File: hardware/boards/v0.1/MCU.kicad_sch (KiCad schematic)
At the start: 38 parts, among them SW24 NRST, SW25 BOOT0, U1 BMDU, U18 STM32H743ZIT6, Y1 ECS-.327-12.5-1210-TR, Y4 8Q-25.000MEEV-T

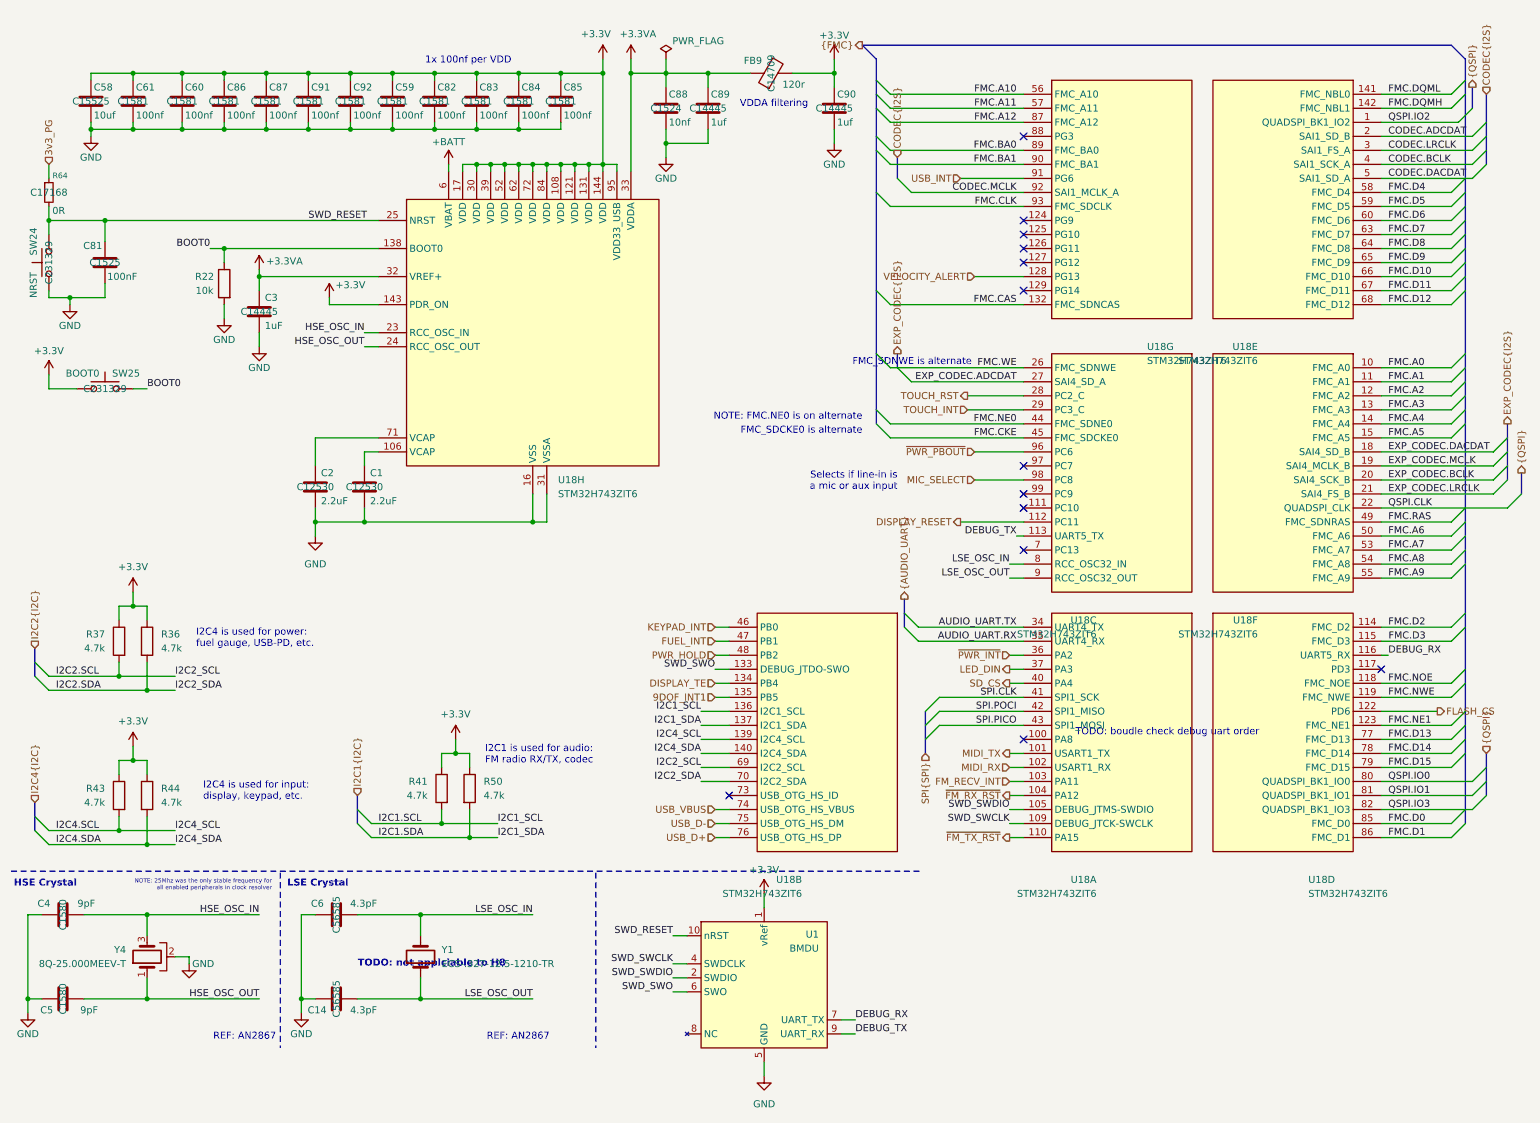
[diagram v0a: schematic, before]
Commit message: feat: update various components to 0402
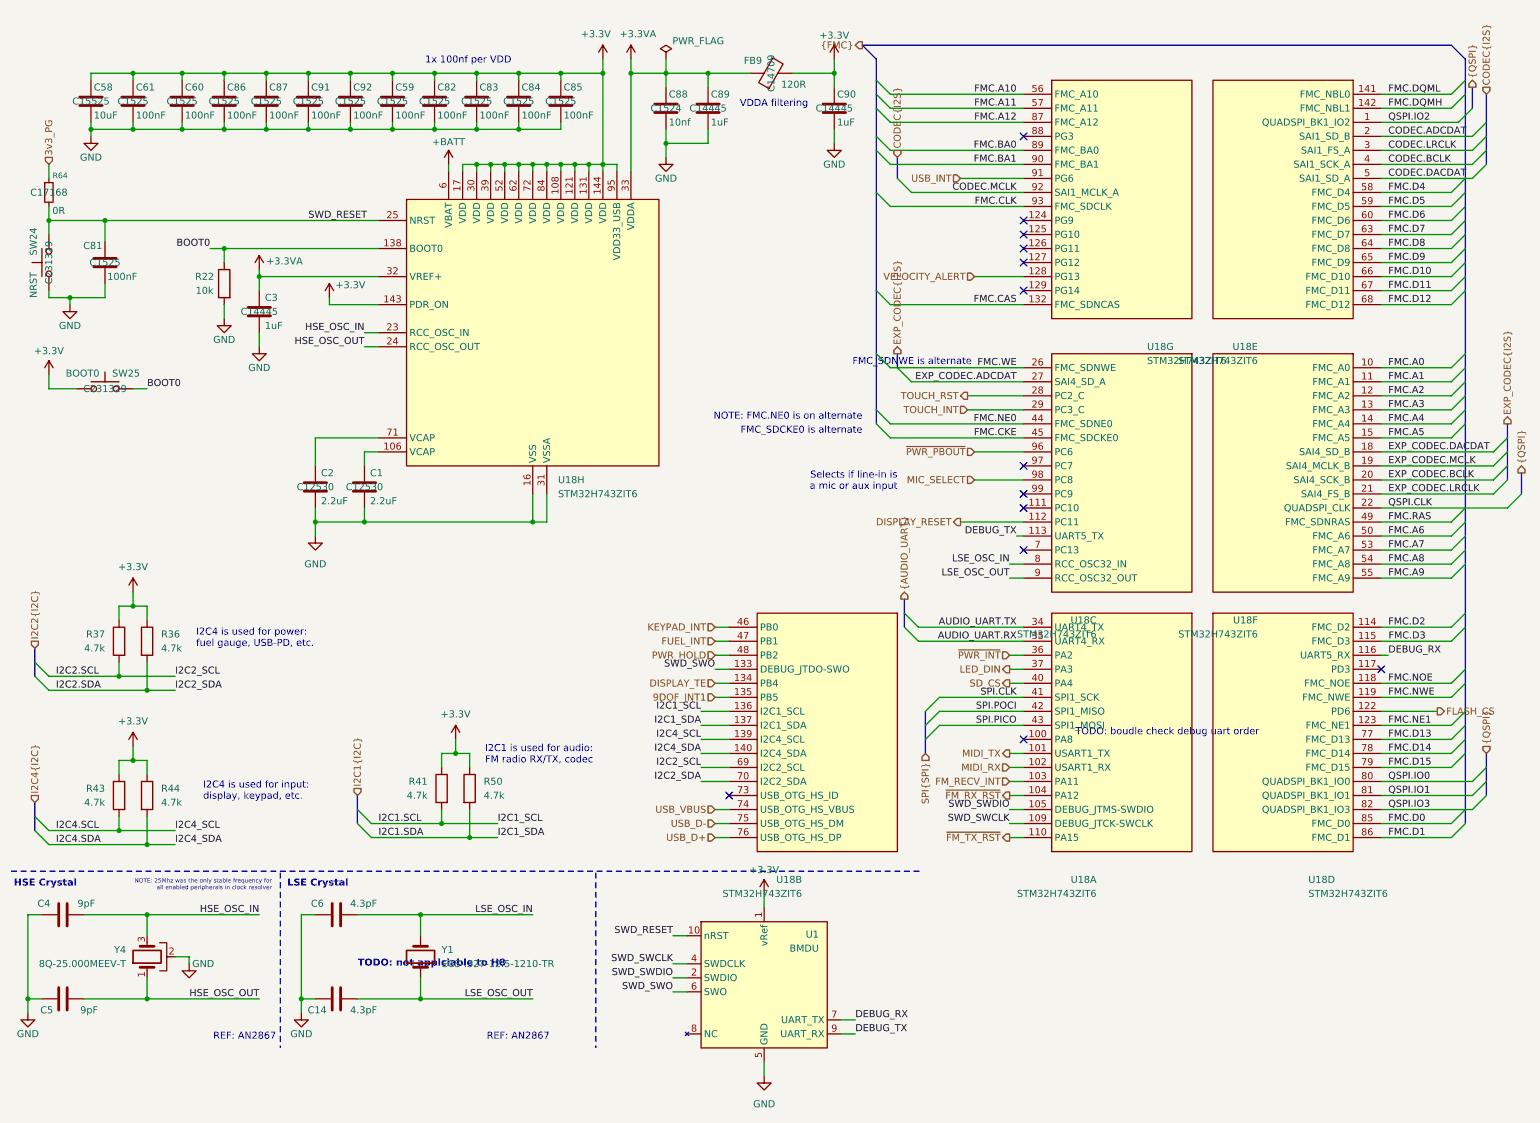
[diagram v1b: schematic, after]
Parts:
- C58: value 10uf -> 10uF
- C59, C60, C61, C82, C83, C84, C85, C86, C87, C91, C92: value 100nf -> 100nF; JLC C1581 -> C1525
- C89, C90: value 1uf -> 1uF
- FB9: value 120r -> 120R

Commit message: feat: various routing cleanup, add SD flash
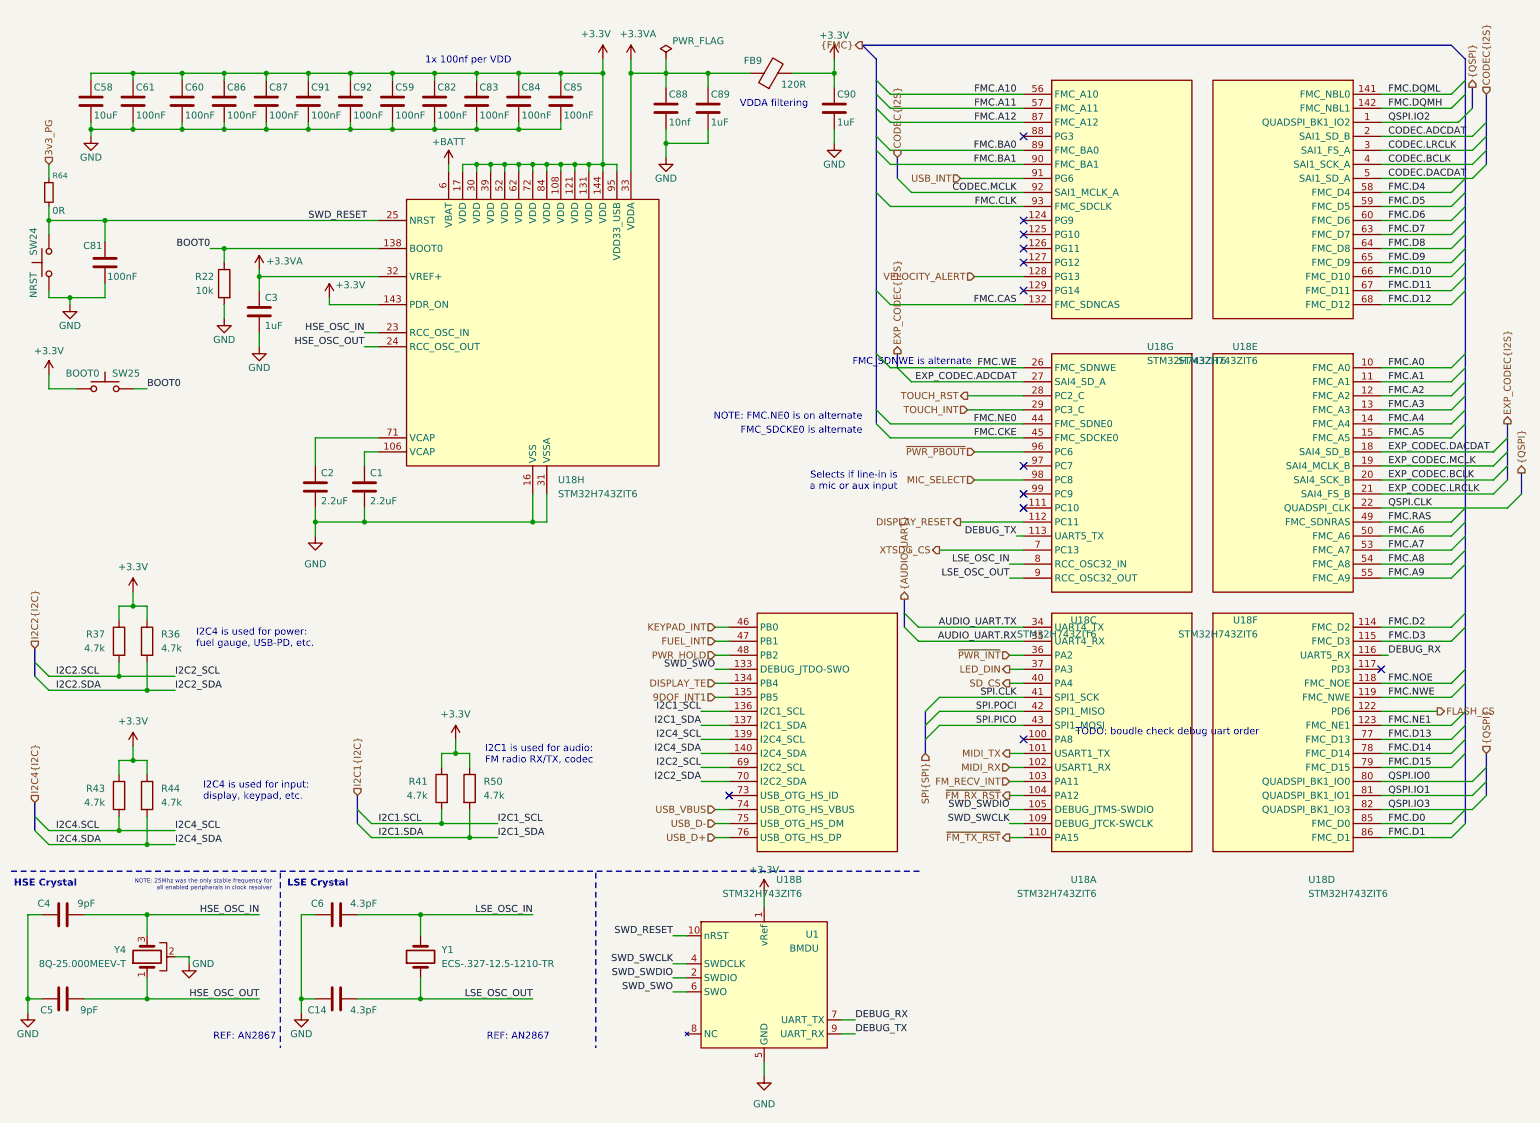
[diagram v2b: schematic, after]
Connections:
- net XTSDG_CS: now reaches U18.7 (PC13)
- no-connect marks 13 -> 12
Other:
- note removed: "TODO: not applciable to H8"

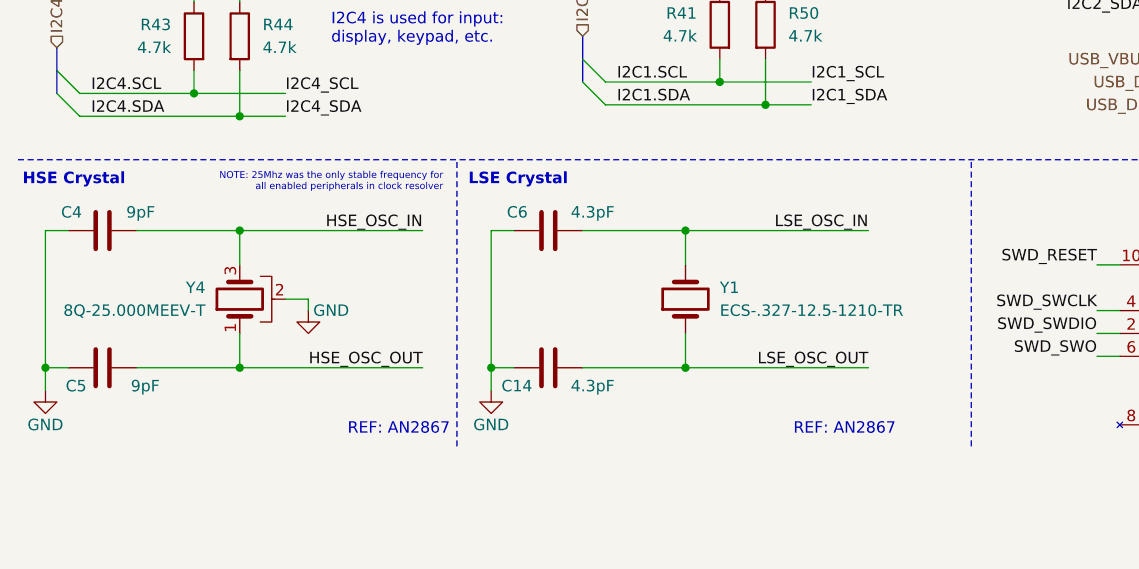
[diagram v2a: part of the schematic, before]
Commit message: feat: swap out of stock components
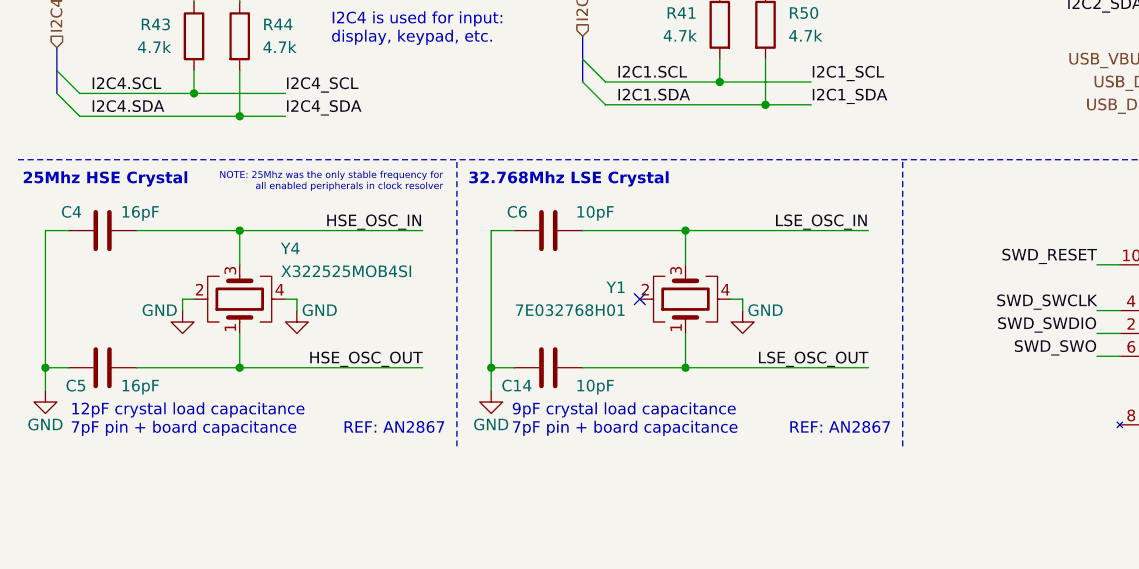
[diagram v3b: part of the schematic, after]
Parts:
- C14, C6: value 4.3pF -> 10pF; JLC C56585 -> C1545
- C4, C5: value 9pF -> 16pF; footprint Capacitor_SMD:C_0402_1005Metric -> Capacitor_SMD:C_0603_1608Metric; JLC C1580 -> C1646
- Y1: value ECS-.327-12.5-1210-TR -> 7E032768H01; footprint pocket_synth:XTAL_ECS-.327-12.5-1210-TR -> pocket_synth:SMD1612-4P; symbol Device:Crystal -> Device:Crystal_GND24; JLC C435179 -> C781734
- Y4: value 8Q-25.000MEEV-T -> X322525MOB4SI; footprint pocket_synth:XTAL_8Q-25.000MEEV-T -> Crystal:Crystal_SMD_3225-4Pin_3.2x2.5mm; symbol Device:Crystal_GND2 -> Device:Crystal_GND24; JLC C2613088 -> C9006
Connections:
- net GND: now also Y1.4, Y4.4
- net LSE_OSC_IN: now also Y1.3; no longer Y1.2
- no-connect marks 12 -> 13
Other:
- note added: "12pF crystal load capacitance 7pF pin + board capacitance"
- note added: "25Mhz HSE Crystal"
- note added: "32.768Mhz LSE Crystal"
- note added: "9pF crystal load capacitance 7pF pin + board capacitance"
- note removed: "HSE Crystal"
- note removed: "LSE Crystal"

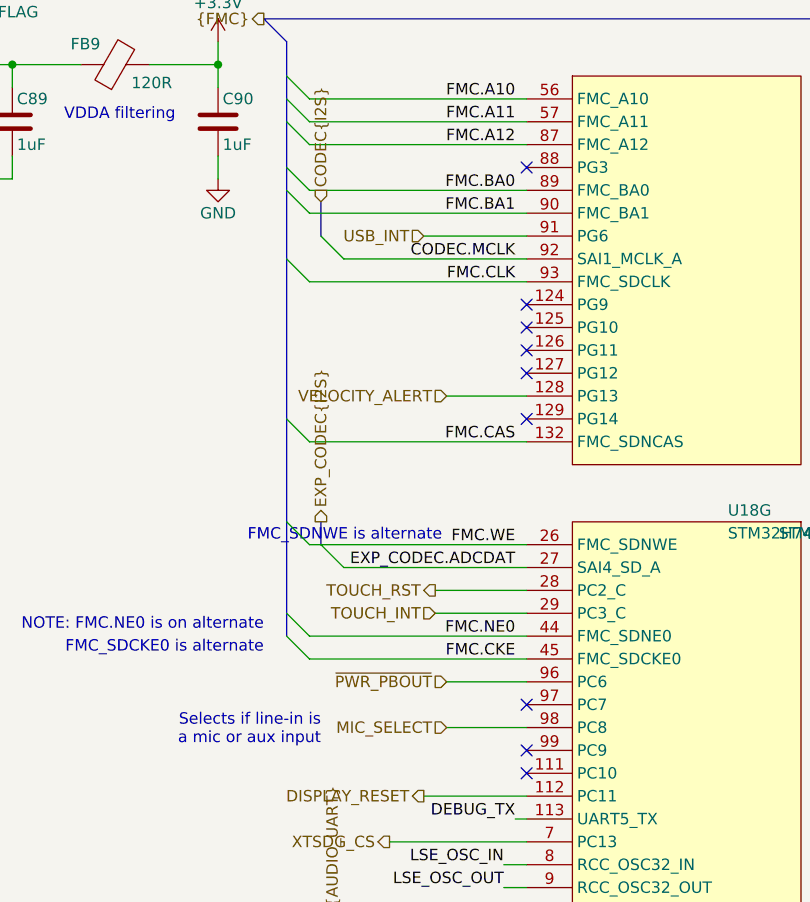
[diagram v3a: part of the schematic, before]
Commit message: feat: various cleanup and BOM adjustment, split audio in into two switches
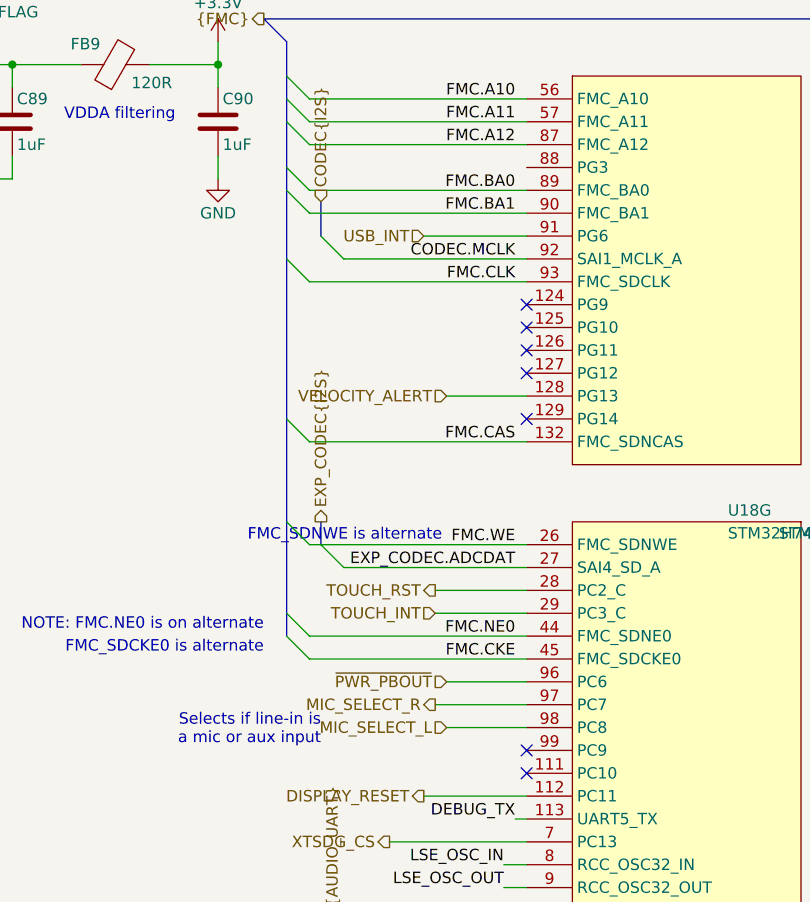
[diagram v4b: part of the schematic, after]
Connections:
- net MIC_SELECT_R: now reaches U18.97 (PC7)
- net MIC_SELECT renamed MIC_SELECT_L
- no-connect marks 13 -> 11

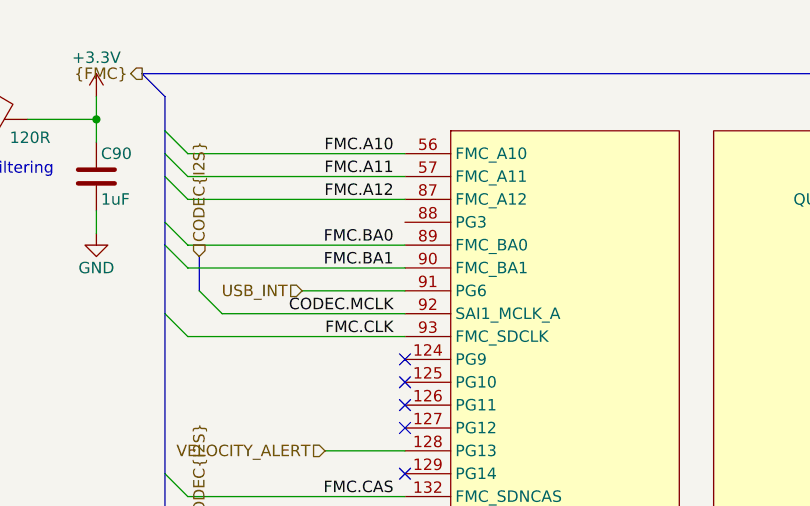
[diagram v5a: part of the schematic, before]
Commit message: feat: add haptic transducer DAC
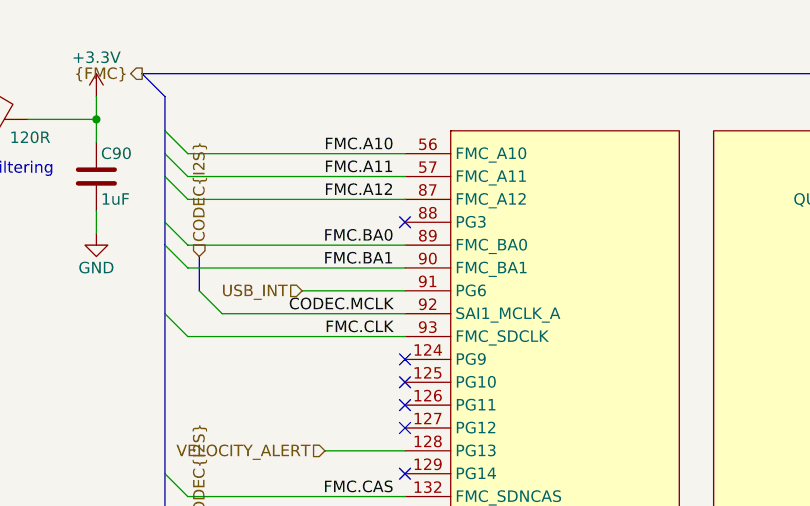
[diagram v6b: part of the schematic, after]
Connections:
- no-connect marks 11 -> 12
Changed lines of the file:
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@@
+	)
+	(no_connect
+		(at 195.58 33.02)
 	)
 	(no_connect

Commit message: chore: schematic cleanup
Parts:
- C88: JLC C1524 -> C15195
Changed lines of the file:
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@@
 			)
 		)
-		(property "JLC" "C1524"
+		(property "JLC" "C15195"
 			(at 130.81 27.94 0)
 			(effects
